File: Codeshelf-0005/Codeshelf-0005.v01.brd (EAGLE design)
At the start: 140.6 x 104 mm, 50 parts, among them J1 M05X2PTH, J2 RJ45-8PTH, J4 RJ45-8PTH, J5 HEADER-2X-2.54MM, U1 ZSFM201-1A, U2 MAX232SOIC16, U3 RS485SOIC, U4 ULN2003AD

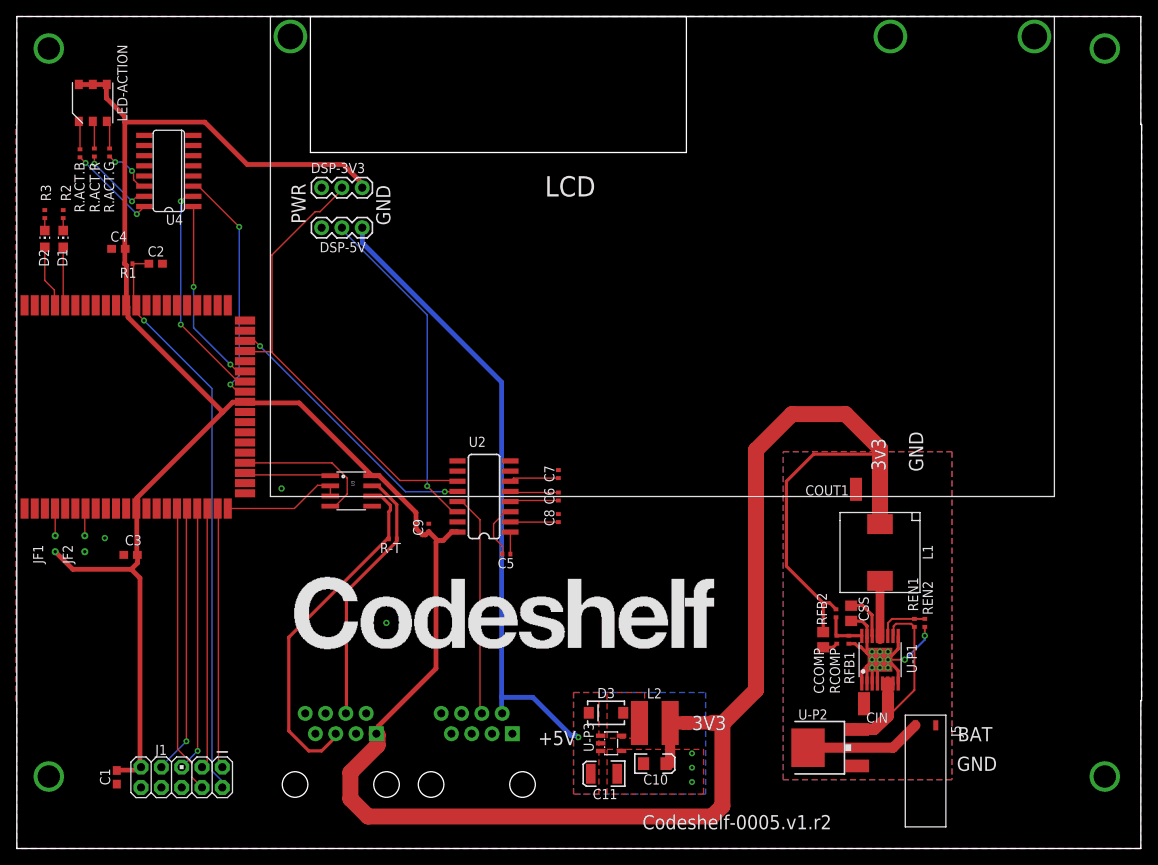
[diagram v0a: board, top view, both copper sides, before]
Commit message: Flip the JTAG port
flip the JTAG port.
Change the LCD holes from pads to drills.
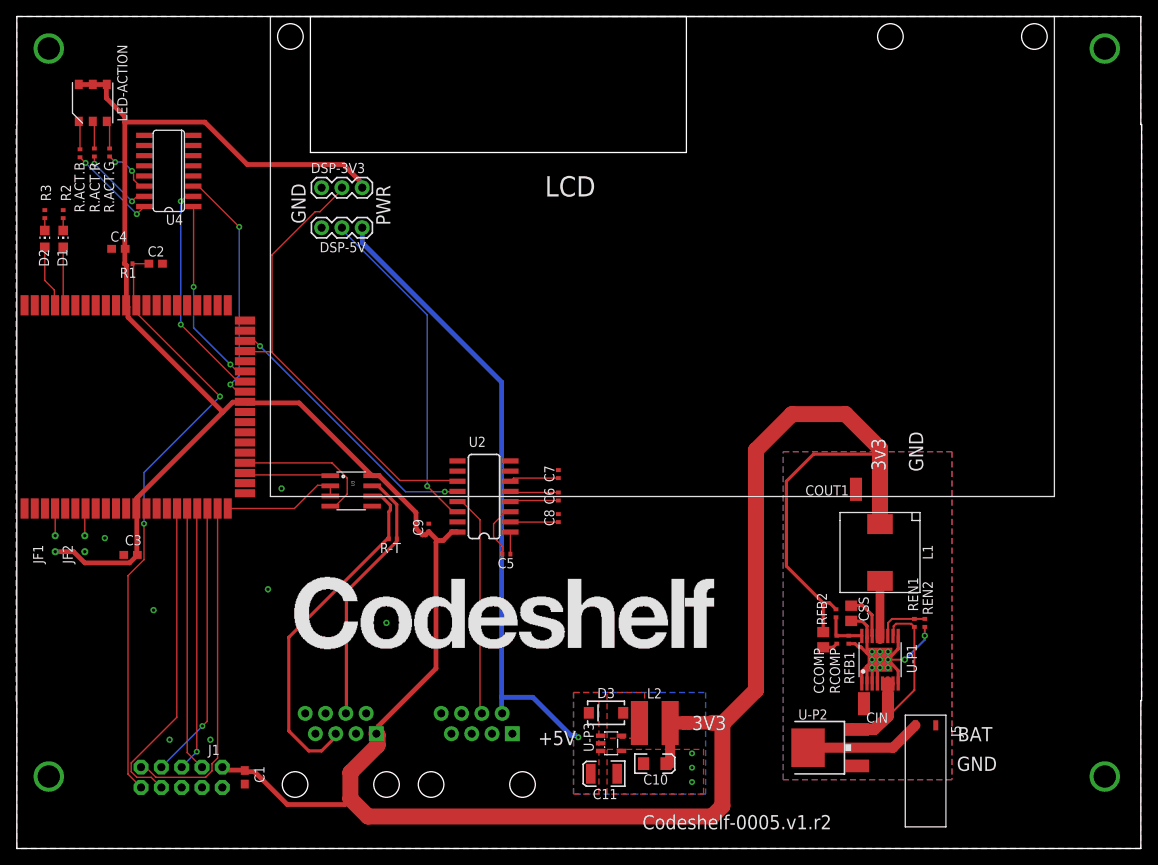
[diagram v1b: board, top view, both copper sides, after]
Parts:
- moved C1 16.0 mm to (38.0, 8.90)
- flipped J1 to the bottom
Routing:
- net +3V3: track 409.9 -> 398.4 mm
- net TMS: track 32.7 -> 42.8 mm
- net RESET: track 72.2 -> 77.5 mm, vias 1 -> 2
- net RTCK: track 36.2 -> 39.9 mm
- net TCK: track 32.7 -> 34.7 mm, vias 0 -> 1
- net TDO: track 33.8 -> 33.1 mm, vias 1 -> 0
- net GND: vias 17 -> 21
